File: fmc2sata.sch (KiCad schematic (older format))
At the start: 11 parts

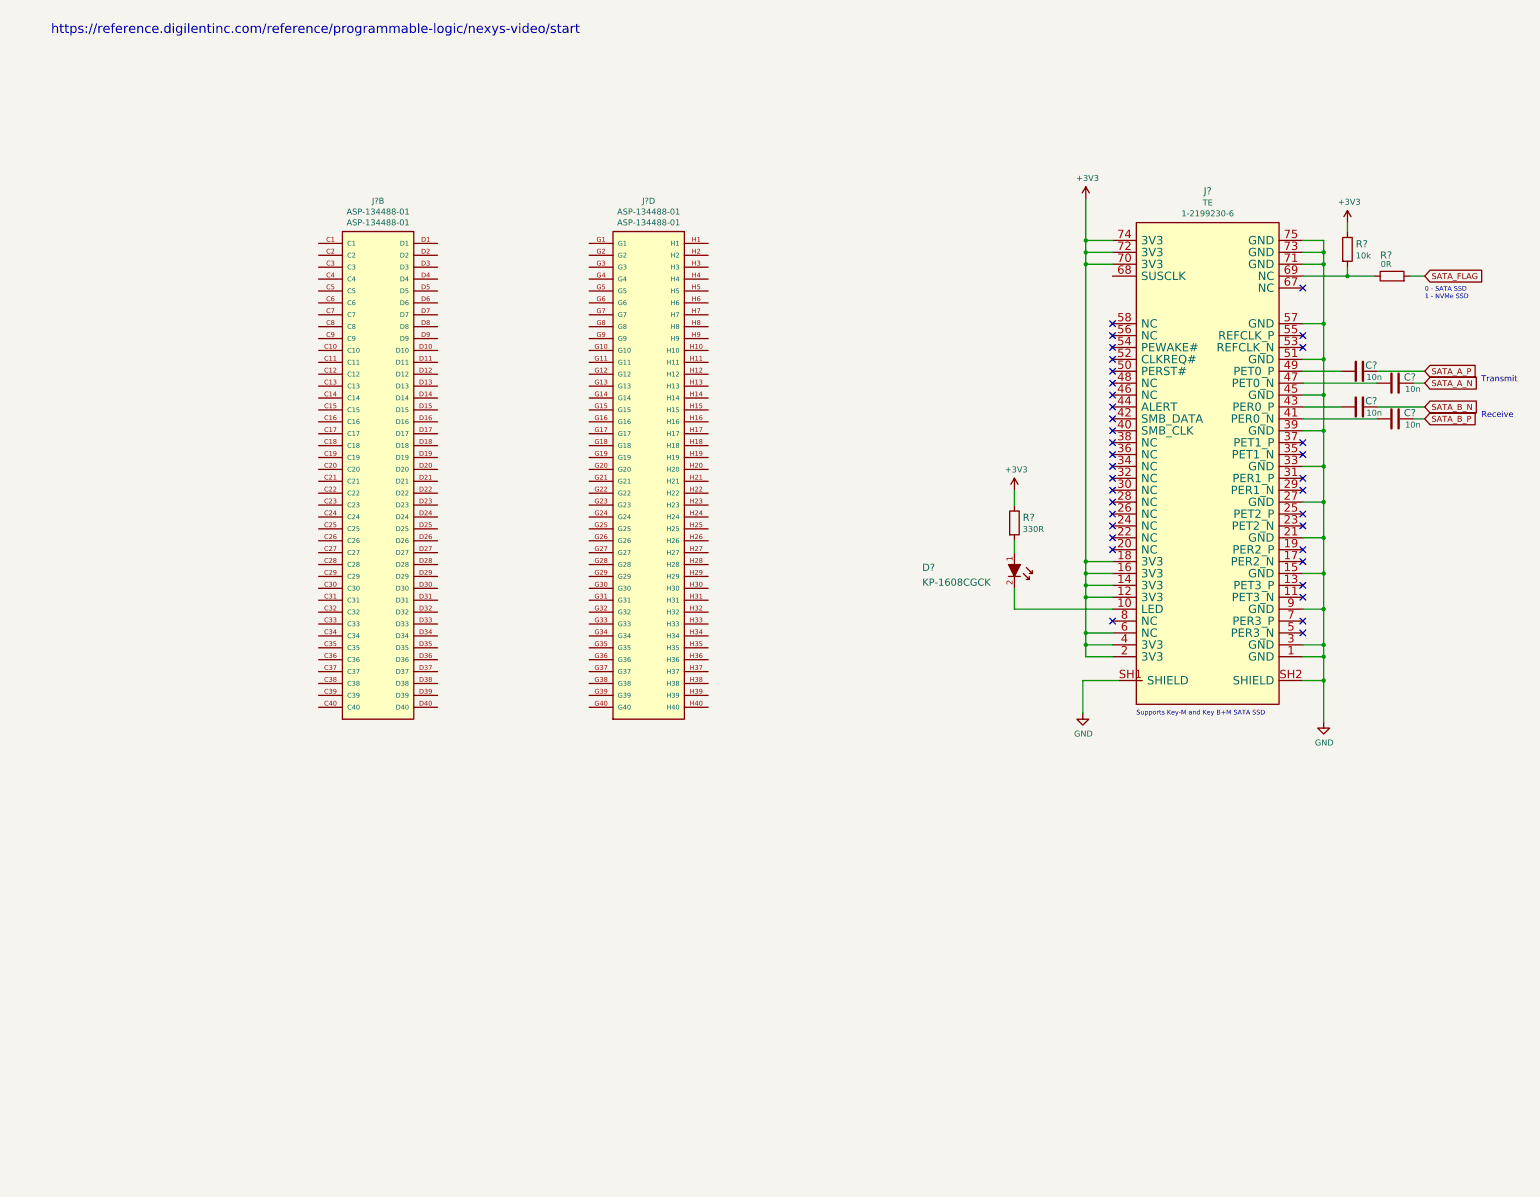
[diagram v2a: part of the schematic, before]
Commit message: Add DC/DC converters
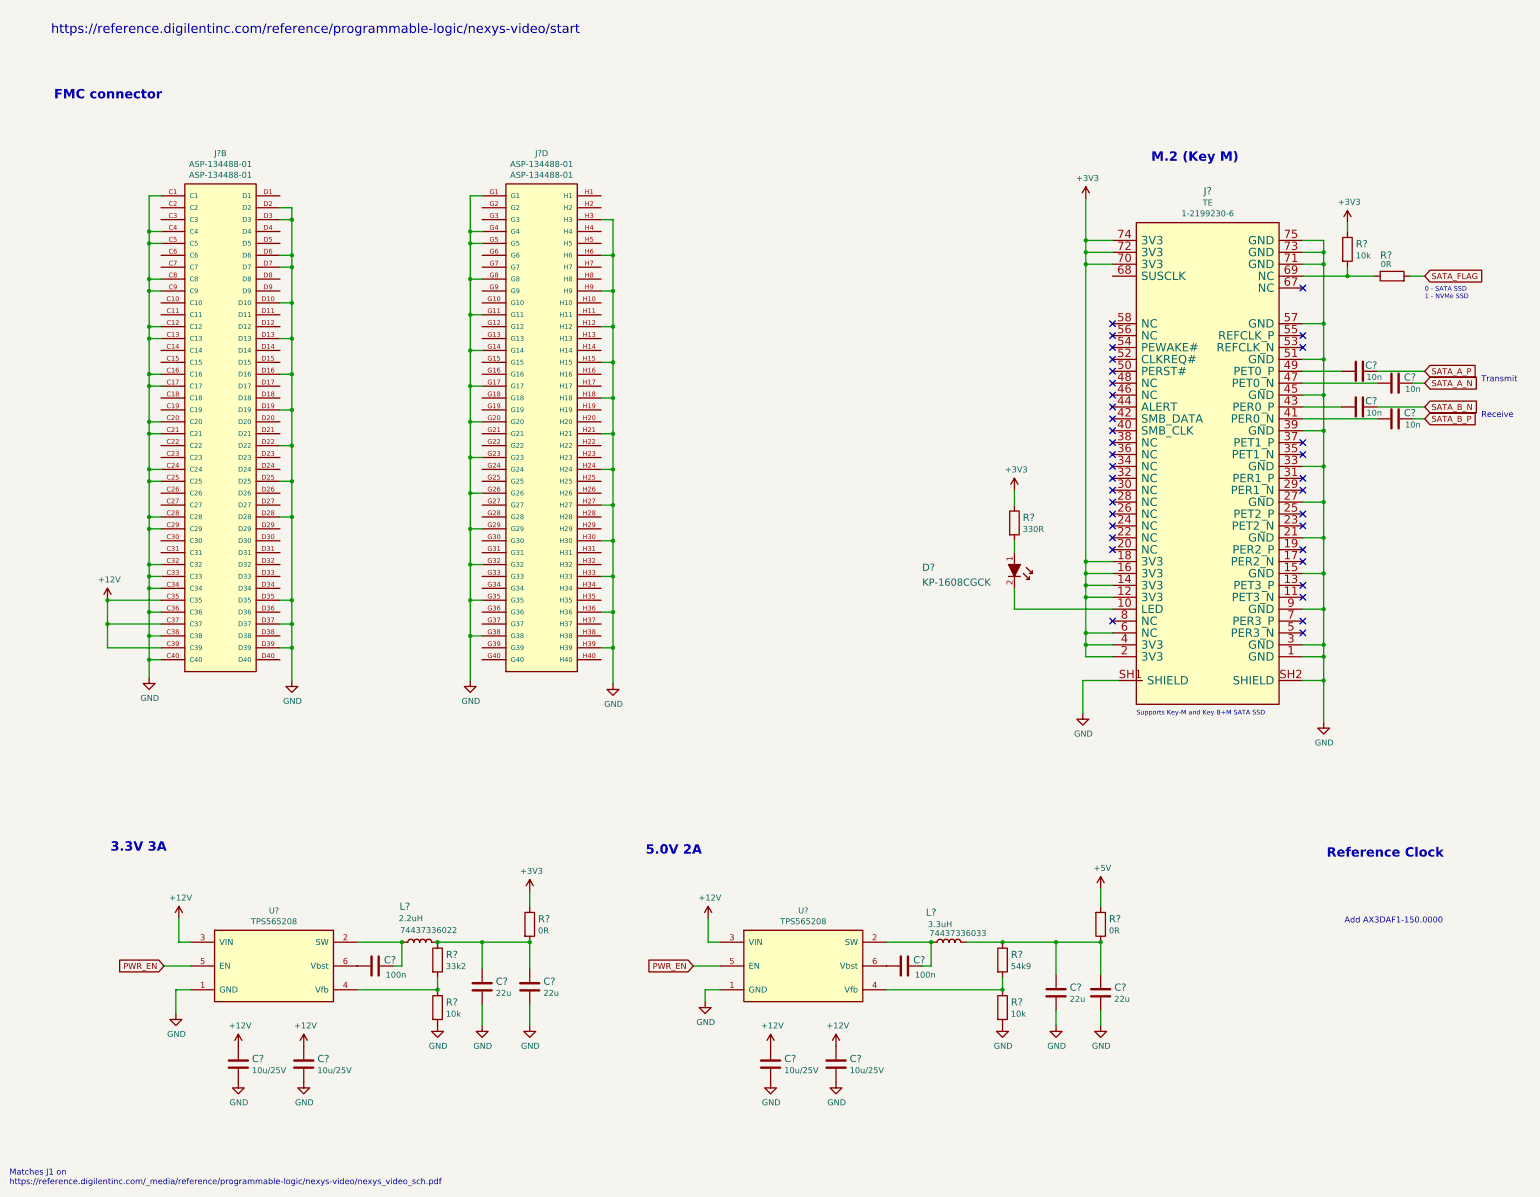
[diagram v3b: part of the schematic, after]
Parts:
- added C? (x2): C_100n_0603, antmicro-footprints:0603-cap, symbol antmicroCapacitors0603:C_100n_0603
- added C? (x4): C_22u_0805_10V, antmicro-footprints:0805-cap, symbol antmicroCapacitorsmisc:C_22u_0805_10V
- added C? (x4): C_10u_25V_0603, antmicro-footprints:0603-cap, symbol antmicroCapacitors0603:C_10u_25V_0603
- added L?: WE_74437336033, antmicro-footprints:WE_74437336033, symbol antmicroFixedInductors:WE_74437336033
- added L?: WE_74437336022, antmicro-footprints:WE_74437336022, symbol antmicroFixedInductors:WE_74437336022
- added R? (x2): R_10k_0402, antmicro-footprints:0402-res, symbol antmicroResistors0402:R_10k_0402
- added R?: R_54k9_0402, antmicro-footprints:0402-res, symbol antmicroResistors0402:R_54k9_0402
- added R?: R_33k2_0402, antmicro-footprints:0402-res, symbol antmicroResistors0402:R_33k2_0402
- added R? (x2): R_0R_0402, antmicro-footprints:0402-res, symbol antmicroResistors0402:R_0R_0402
- added U? (x2): TPS565208, antmicro-footprints:SOT-23-6, symbol antmicroPMICVoltageRegulatorsDCDCSwitchingRegulators:TPS565208
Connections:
- net +3V3: now also R?.1
- net GND: now also J?.C1, J?.C12, J?.C13, J?.C16, J?.C17, J?.C20, J?.C21, J?.C24, J?.C25, J?.C28, J?.C29, J?.C32, J?.C33, J?.C34, J?.C36, J?.C38, J?.C4, J?.C40, J?.C5, J?.C8, J?.C9, J?.D10, J?.D13, J?.D16, J?.D19, J?.D2, J?.D22, J?.D25, J?.D28, J?.D3, J?.D35, J?.D37, J?.D39, J?.D6, J?.D7, J?.G1, J?.G11, J?.G14, J?.G17, J?.G20, J?.G23, J?.G26, J?.G29, J?.G32, J?.G35, J?.G38, J?.G4, J?.G5, J?.G8, J?.H12, J?.H15, J?.H18, J?.H21, J?.H24, J?.H27, J?.H3, J?.H30, J?.H33, J?.H36, J?.H39, J?.H6, J?.H9, C?.2, C?.2, C?.2, C?.2, C?.2, C?.2, C?.2, C?.2, R?.2, R?.2, U?.1 (GND), U?.1 (GND)
- net +12V: now reaches J?.C35
- net +12V: now also J?.C37, J?.C39, C?.1, C?.1, C?.1, C?.1, U?.3 (VIN), U?.3 (VIN)
- new net: C?.1, L?.1 (P), U?.2 (SW) (x2)
- new net: R?.1, R?.2, U?.4 (Vfb) (x2)
- new net: C?.2, U?.6 (Vbst) (x2)
- new net: C?.1, C?.1, L?.2 (P), R?.1, R?.1
- new net: C?.1, C?.1, L?.2 (P), R?.1, R?.2
- new net +5V: R?.2
- new net PWR_EN: U?.5 (EN), U?.5 (EN)
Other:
- note added: "3.3V 3A"
- note added: "5.0V 2A"
- note added: "Add AX3DAF1-150.0000"
- note added: "FMC connector"
- note added: "M.2 (Key M)"
- note added: "Matches J1 on\nhttps://reference.digilentinc.com/_media/reference/programmable-logic/nexys-video/nexys_video_sch.pdf"
- note added: "Reference Clock"
- moved on the sheet: J?B, J?D

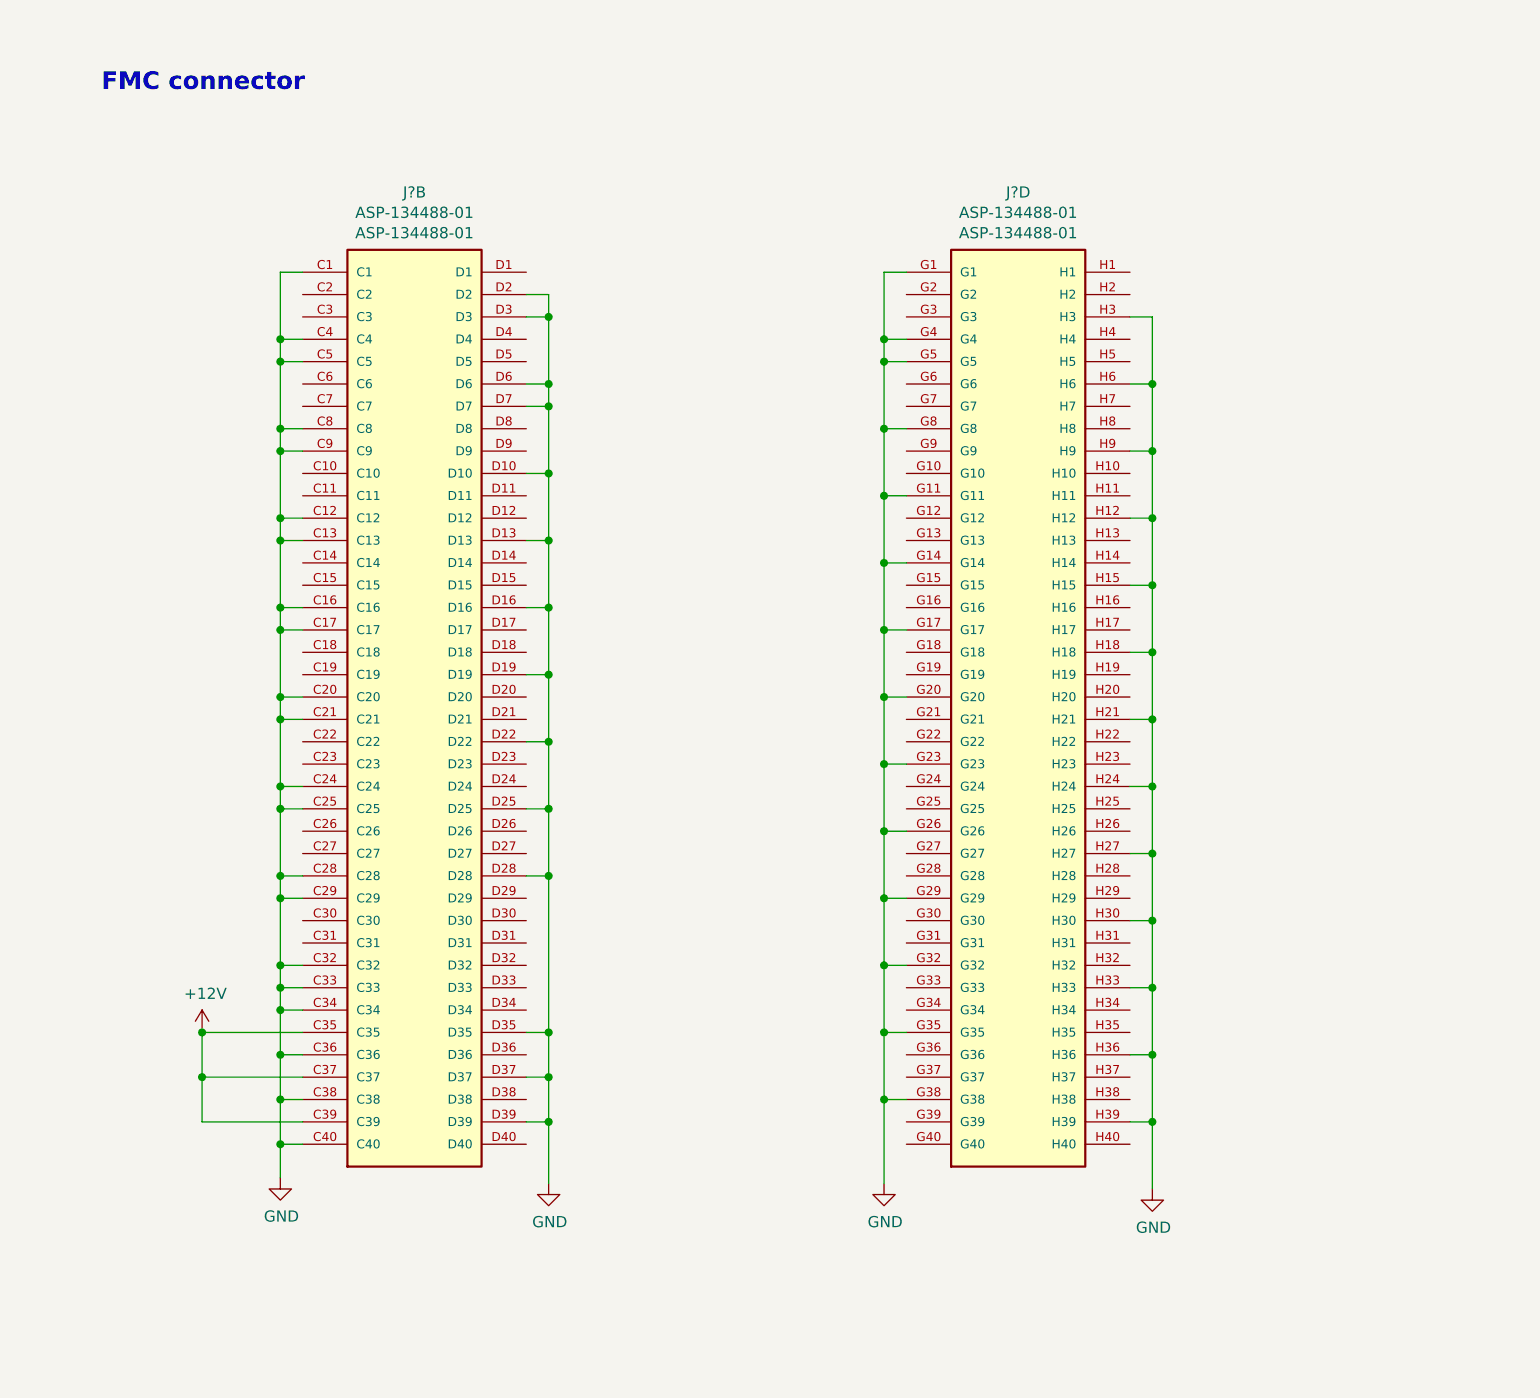
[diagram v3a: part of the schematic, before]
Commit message: Connect SATA lanes
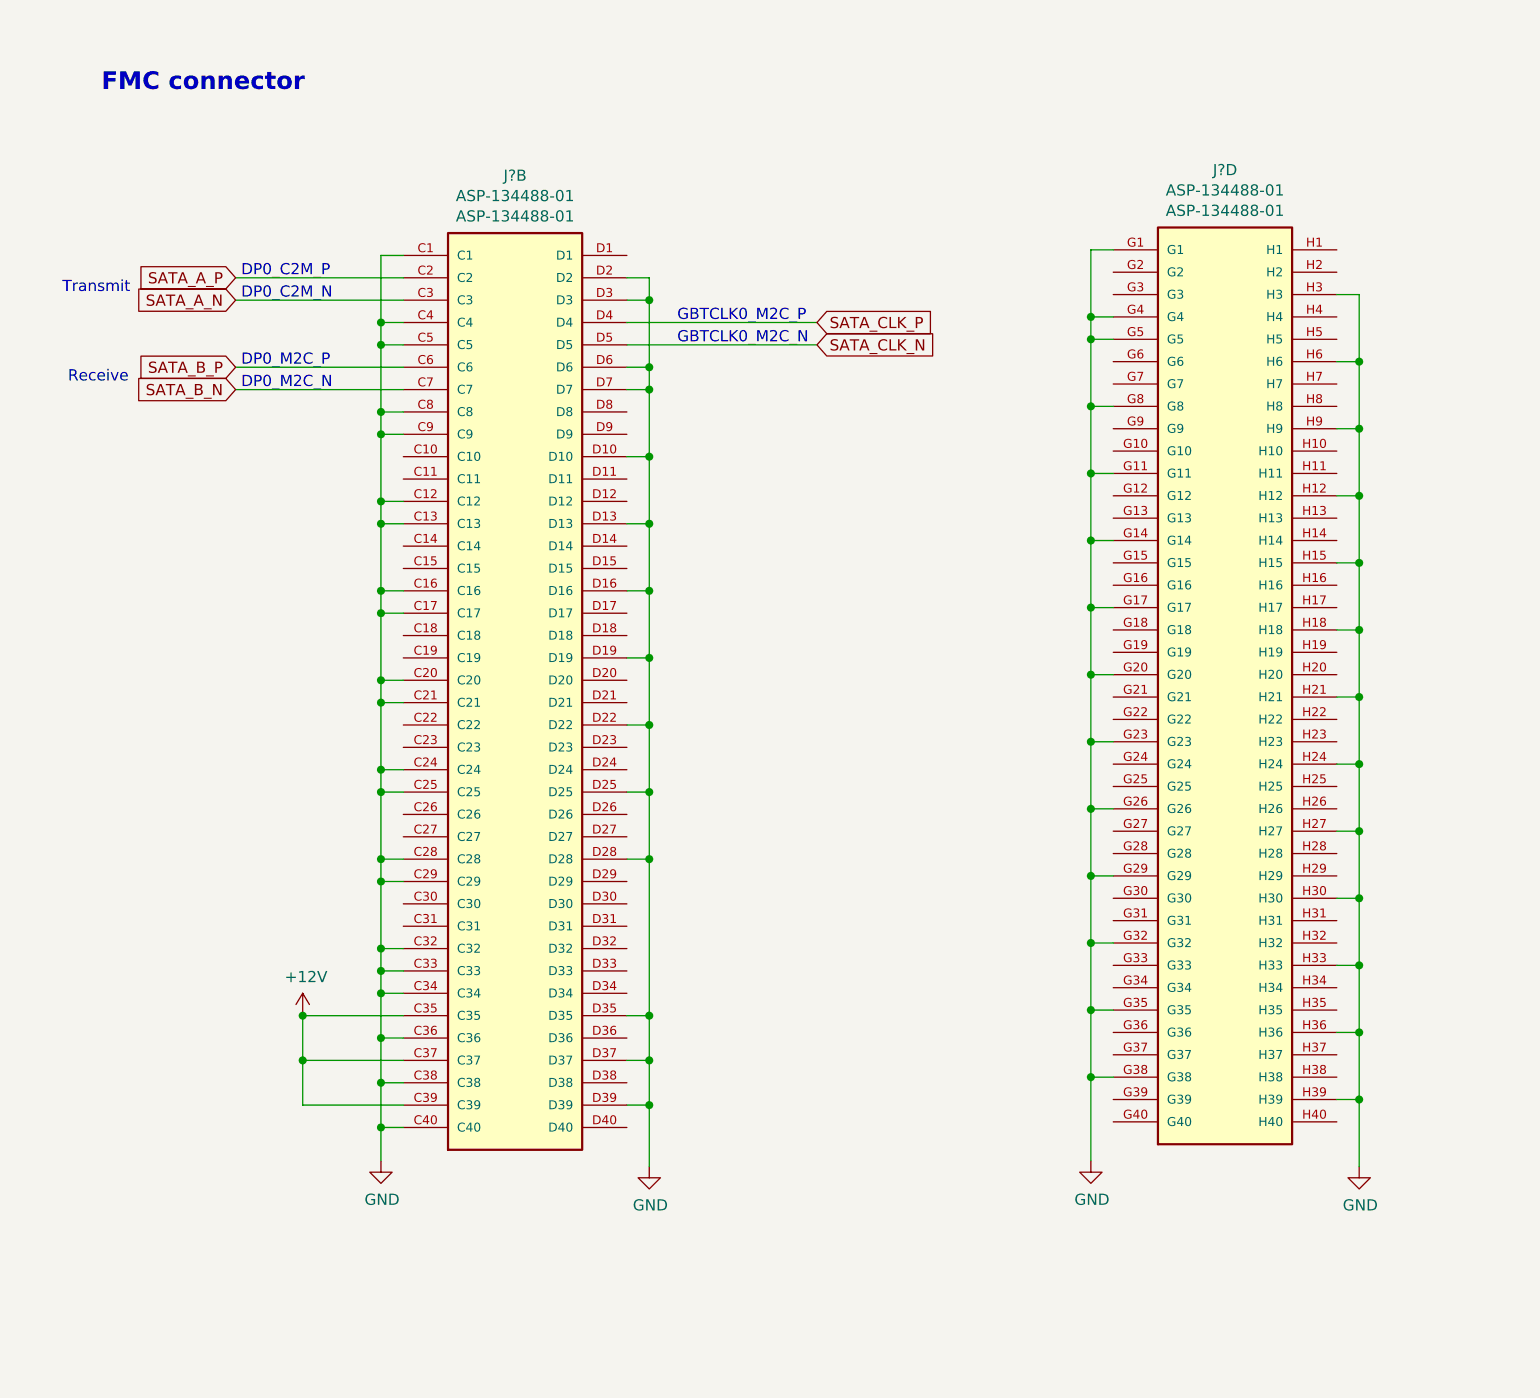
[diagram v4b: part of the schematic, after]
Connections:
- net SATA_A_N: now also J?.C3
- net SATA_A_P: now also J?.C2
- net SATA_B_N: now also J?.C7
- net SATA_B_P: now also J?.C6
- net SATA_CLK_P: now reaches J?.D4
- net SATA_CLK_N: now reaches J?.D5
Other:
- note added: "DP0_C2M_N"
- note added: "DP0_C2M_P"
- note added: "DP0_M2C_N"
- note added: "DP0_M2C_P"
- note added: "GBTCLK0_M2C_N"
- note added: "GBTCLK0_M2C_P"
- moved on the sheet: J?B, J?D

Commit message: Add basic PCB outline
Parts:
- added SP1: 9774025151, antmicro-footprints:9774025151, symbol antmicroMechanicalParts:9774025151
- gave numbers to parts that had none: 30
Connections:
- net GND: now also SP1.1
